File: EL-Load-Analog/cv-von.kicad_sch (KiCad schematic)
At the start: 23 parts, among them Q401 BSS138, U401 AD8038, U402 LM393, U403 74HCT02

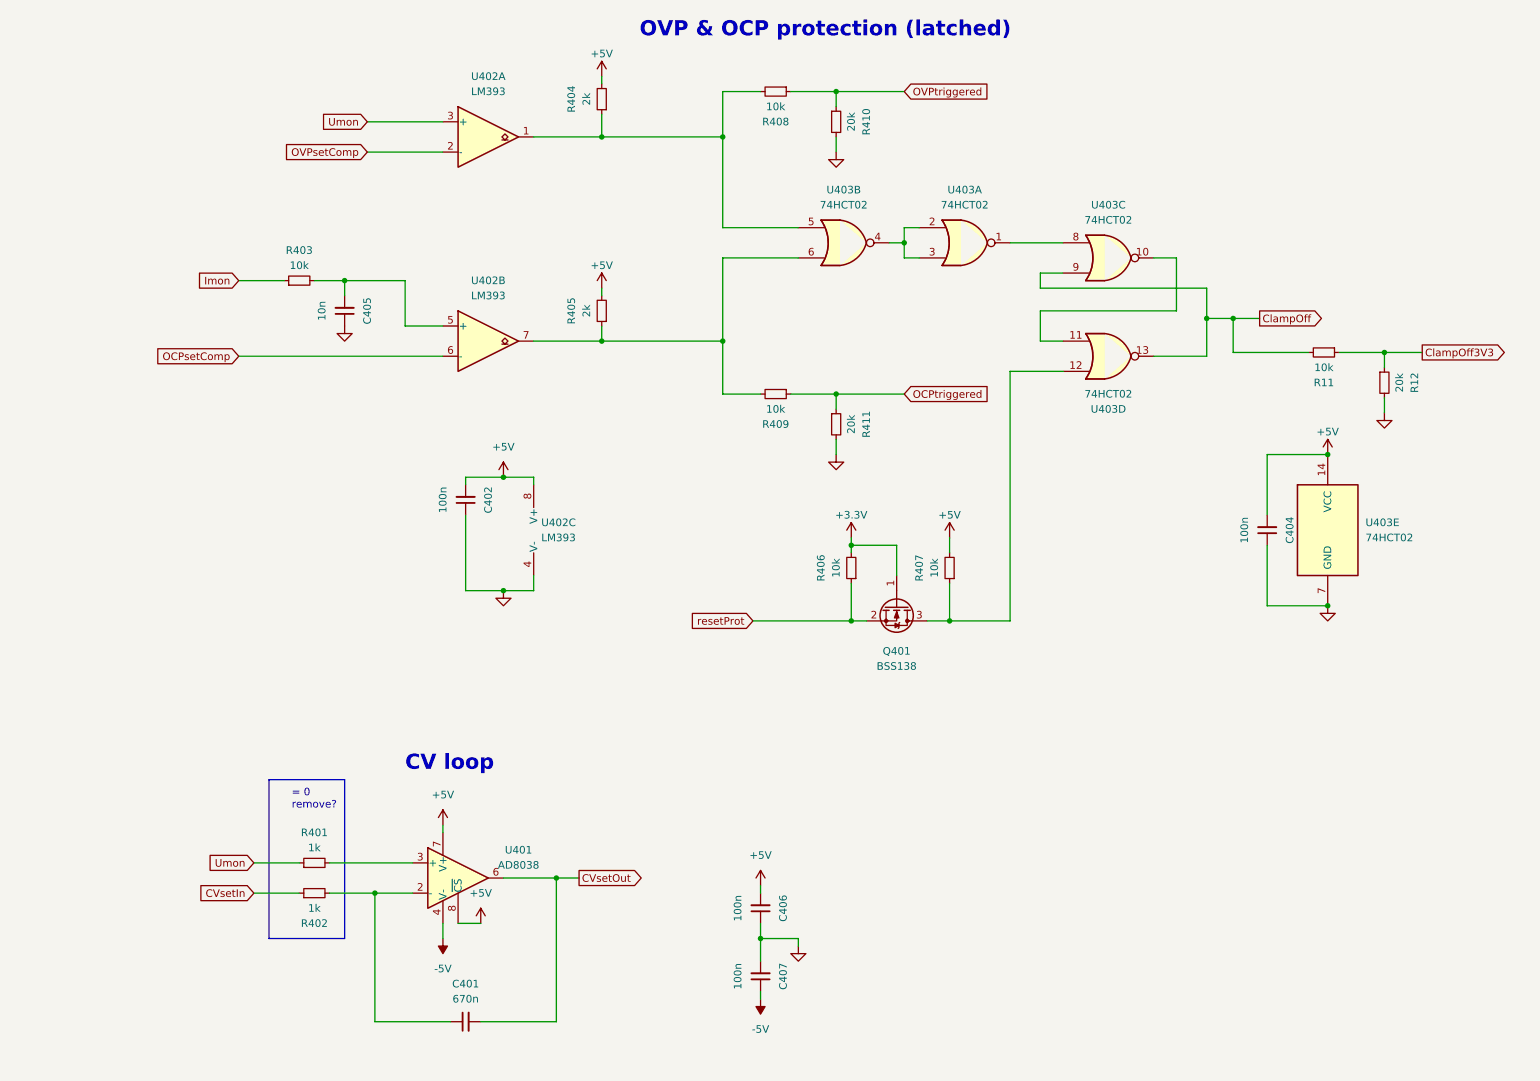
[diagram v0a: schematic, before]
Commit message: Major Analog PCB update DAC/ADC + connectors included, fan IC removed
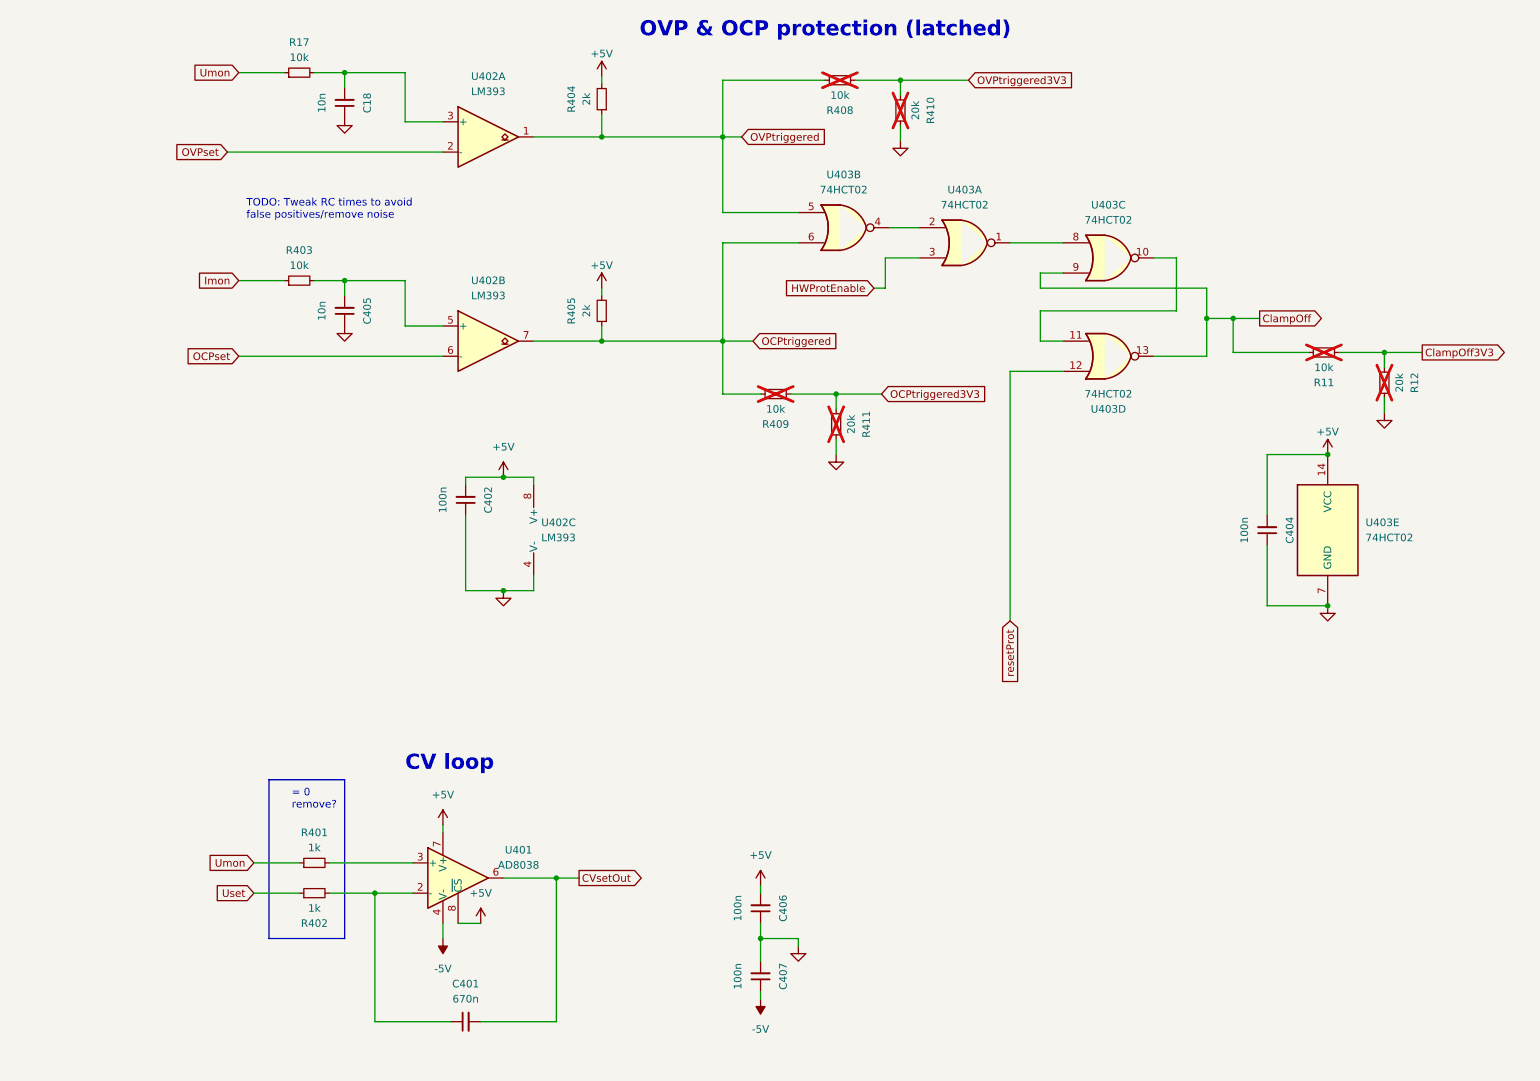
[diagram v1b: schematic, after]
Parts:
- removed Q401: BSS138, Package_TO_SOT_SMD:SOT-23, symbol Transistor_FET:BSS138
- removed R406, R407: 10k, Resistor_SMD:R_0805_2012Metric_Pad1.20x1.40mm_HandSolder, symbol Device:R_Small
- added C18: 10n, Capacitor_SMD:C_0805_2012Metric, symbol Device:C_Small
- added R17: 10k, Resistor_SMD:R_0805_2012Metric, symbol Device:R_Small
- C401, C402, C404, C405, C406, C407: footprint Capacitor_SMD:C_0805_2012Metric_Pad1.18x1.45mm_HandSolder -> Capacitor_SMD:C_0805_2012Metric
- R11, R12, R408, R409, R410, R411: footprint Resistor_SMD:R_0805_2012Metric_Pad1.20x1.40mm_HandSolder -> Resistor_SMD:R_0805_2012Metric; now not fitted; now left out of the parts list
- R401, R402, R403, R404, R405: footprint Resistor_SMD:R_0805_2012Metric_Pad1.20x1.40mm_HandSolder -> Resistor_SMD:R_0805_2012Metric
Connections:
- net GND: now also C18.1
- net OCPtriggered: now also R405.1, R409.2, U402.7, U403.6; no longer R409.1, R411.1
- net OVPtriggered: now also R404.1, R408.2, U402.1, U403.5; no longer R408.1, R410.1
- net Umon: now also R17.1; no longer U402.3 (+)
- net resetProt: now also U403.12
- net at U403.2, U403.4: no longer U403.3
- net CVsetIn renamed Uset
- net OCPsetComp renamed OCPset
- net OVPsetComp renamed OVPset
- new net: C18.2, R17.2, U402.3 (+)
- new net HWProtEnable: U403.3
- new net OCPtriggered3V3: R409.1, R411.1
- new net OVPtriggered3V3: R408.1, R410.1
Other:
- note added: "TODO: Tweak RC times to avoid false positives/remove noise"
- moved on the sheet: U403B

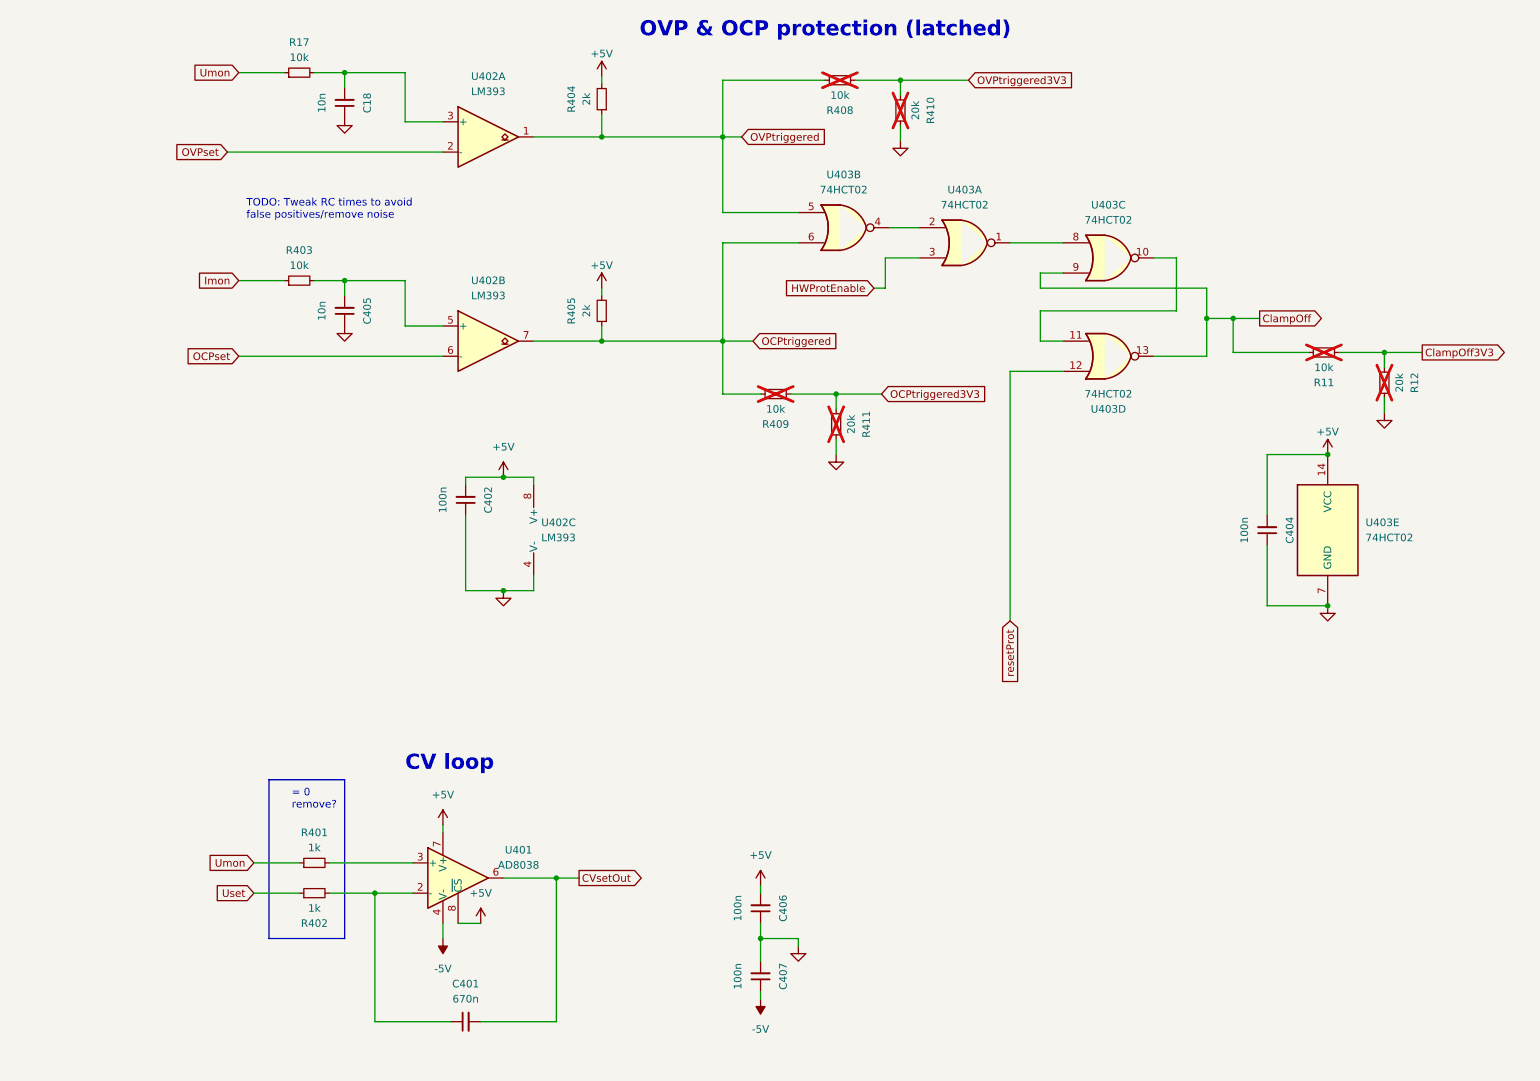
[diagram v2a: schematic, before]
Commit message: Added SenseError detection (including ocmponents), added clearances, fixed few BOM items.
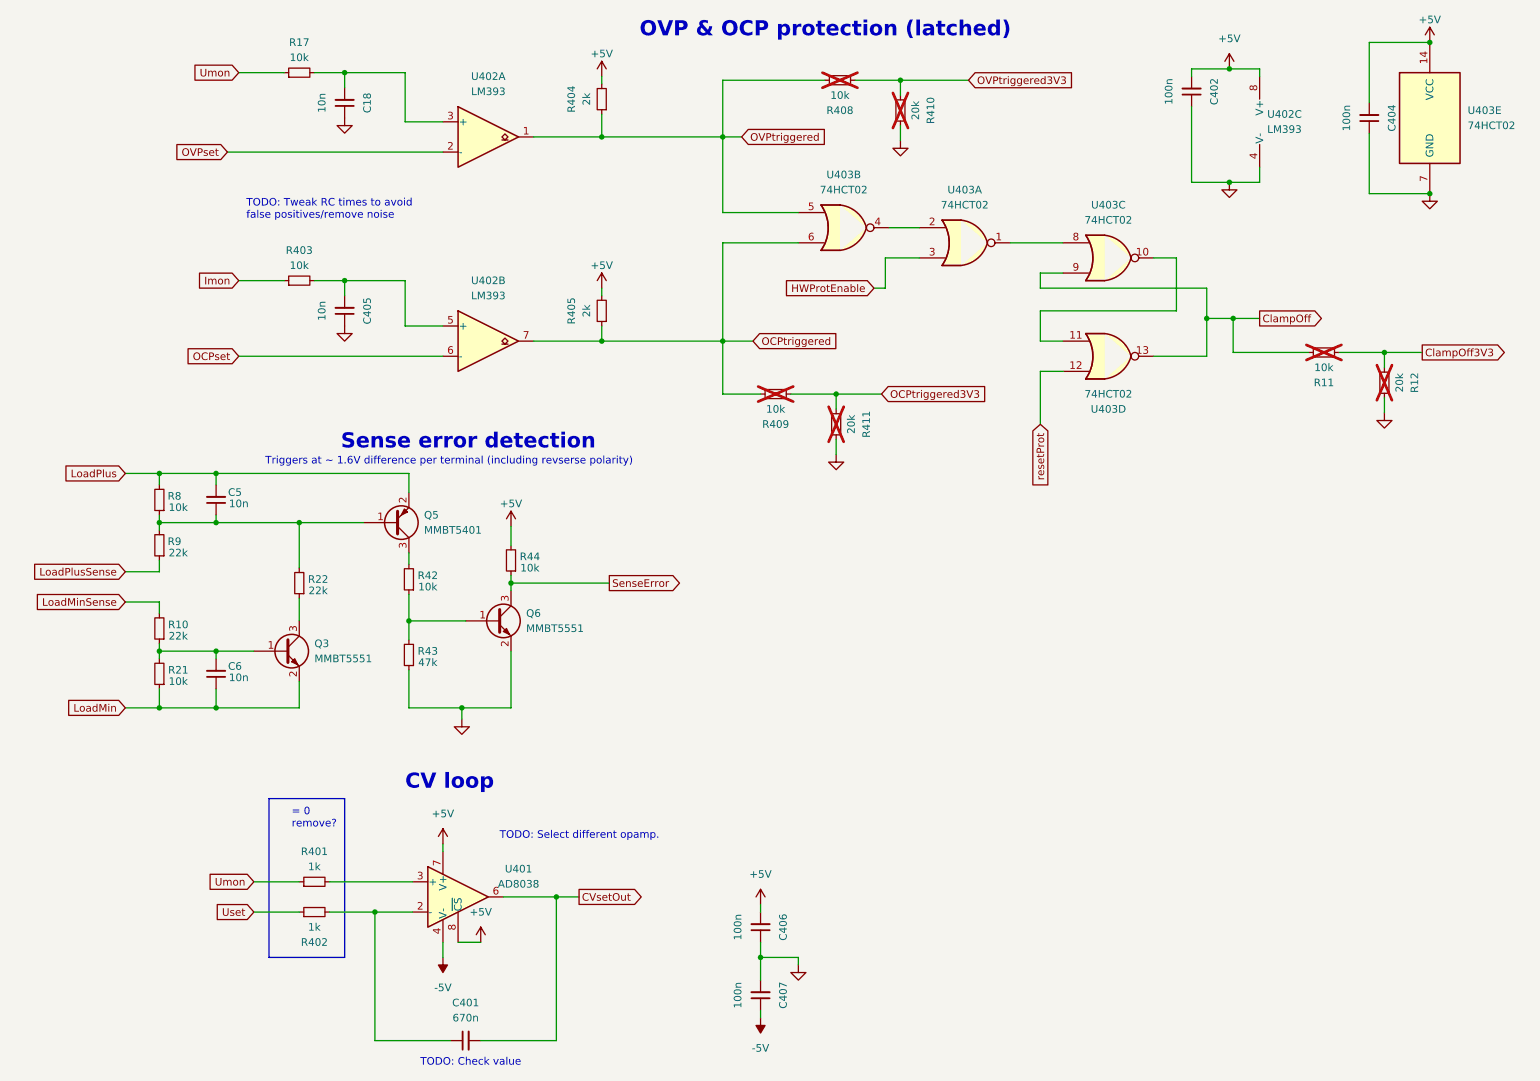
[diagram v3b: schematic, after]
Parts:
- added C5, C6: 10n, Capacitor_SMD:C_0805_2012Metric, symbol Device:C_Small
- added Q3, Q6: MMBT5551, Package_TO_SOT_SMD:SOT-23, symbol EL-Load:MMBT5551
- added Q5: MMBT5401, Package_TO_SOT_SMD:SOT-23, symbol EL-Load:MMBT5401
- added R10, R22, R9: 22k, Resistor_SMD:R_0805_2012Metric, symbol Device:R_Small
- added R21, R42, R44, R8: 10k, Resistor_SMD:R_0805_2012Metric, symbol Device:R_Small
- added R43: 47k, Resistor_SMD:R_0805_2012Metric, symbol Device:R_Small
- C18, C405: Part Name (none) -> C_10.0nF_0805_20%
- C402, C404, C406, C407: Part Name (none) -> C_100.0nF_0805_20%
- R11, R17, R403, R408, R409: Part Name (none) -> R_10.0kΩ_0805_1%
- R12, R410, R411: Part Name (none) -> R_20.0kΩ_0805_1%
- R401, R402: Part Name (none) -> R_1.0kΩ_0805_1%
- R404, R405: Part Name (none) -> R_2.0kΩ_0805_1%
- U401: Part Name (none) -> U_AD8038ARZ
- U402: Part Name (none) -> U_LM393
- U403: Part Name (none) -> U_74HCT02D
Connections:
- net +5V: now also R44.2
- net GND: now also Q6.2 (E), R43.1
- new net: C5.1, Q5.1 (B), R22.2, R8.1, R9.2
- new net: Q6.1 (B), R42.1, R43.2
- new net: Q5.3 (C), R42.2
- new net: Q3.3 (C), R22.1
- new net: C6.2, Q3.1 (B), R10.1, R21.2
- new net LoadMin: C6.1, Q3.2 (E), R21.1
- new net LoadMinSense: R10.2
- new net LoadPlus: C5.2, Q5.2 (E), R8.2
- new net LoadPlusSense: R9.1
- new net SenseError: Q6.3 (C), R44.1
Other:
- note added: "Sense error detection"
- note added: "TODO: Check value"
- note added: "TODO: Select different opamp."
- note added: "Triggers at ~ 1.6V difference per terminal (including revserse polarity)"
- moved on the sheet: C401, C402, C404, C406, C407, R401, R402, U401, U402C, U403E
